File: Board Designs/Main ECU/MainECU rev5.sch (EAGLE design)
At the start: 164 parts, among them Q10 MMBT3904LT3G, Q11 MMBT3904LT3G, Q9 MMBT3904LT3G, X1 CONNECTOR-37, X2 CONNECTOR-4AUTOSPORT, X3 CONNECTOR-4NANO-FIT-VERTICAL-4, X4 CONNECTOR-4NANO-FIT-VERTICAL-4

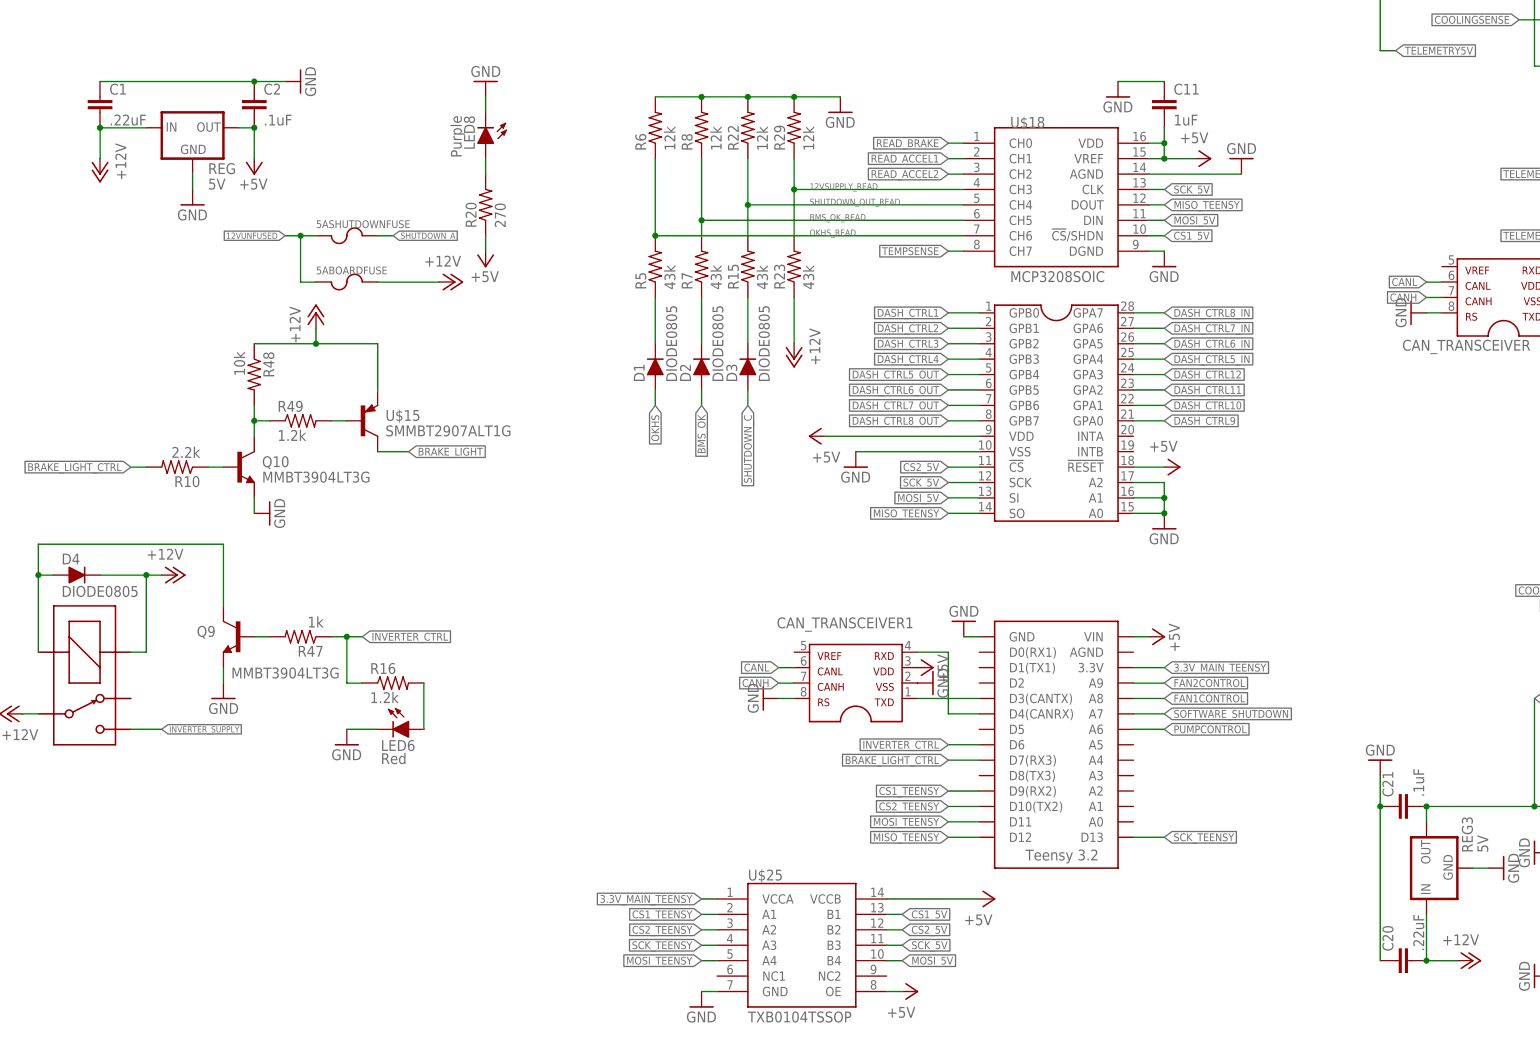
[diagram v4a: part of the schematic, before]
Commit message: Main ECU rev{1-5}: Update values of OKI-78SR capacitors to 10uF
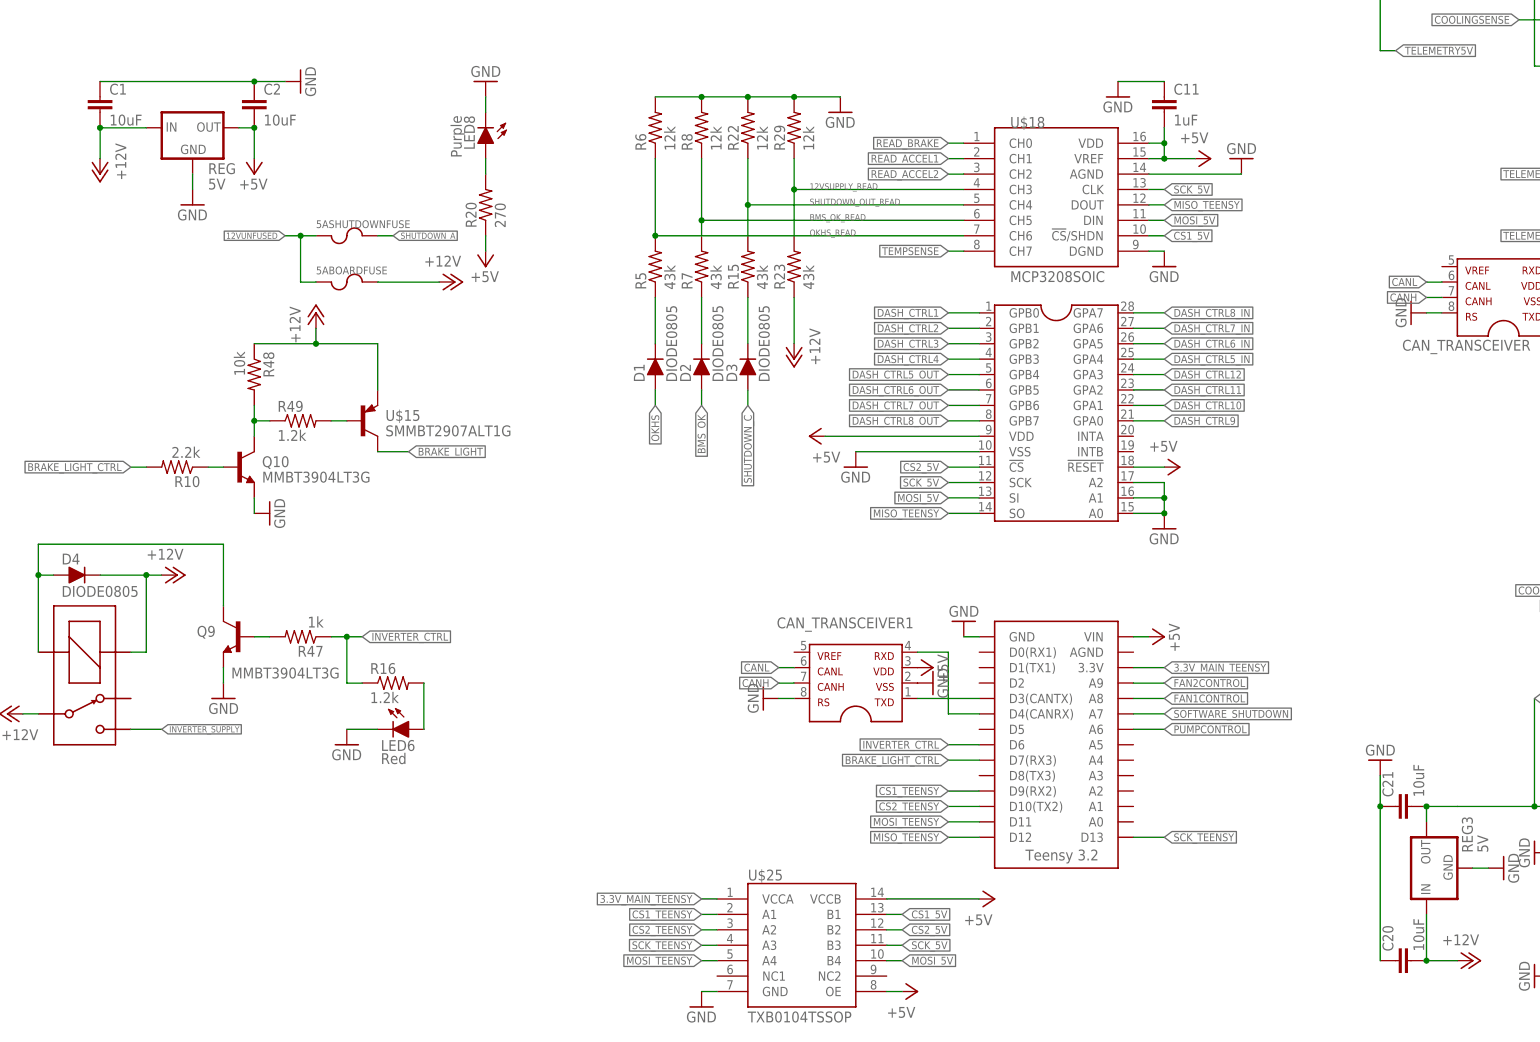
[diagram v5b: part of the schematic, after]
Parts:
- C1, C20: value .22uF -> 10uF
- C2, C21: value .1uF -> 10uF
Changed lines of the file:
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@@
 <part name="REG" library="HyTechDevices" deviceset="OKI-78SR" device="" value="5V"/>
 <part name="GND9" library="HyTechSymbols" deviceset="GND" device=""/>
-<part name="C1" library="HyTechDevices" deviceset="CAP" device="0805" value=".22uF"/>
-<part name="C2" library="HyTechDevices" deviceset="CAP" device="0805" value=".1uF"/>
+<part name="C1" library="HyTechDevices" deviceset="CAP" device="0805" value="10uF"/>
+<part name="C2" library="HyTechDevices" deviceset="CAP" device="0805" value="10uF"/>
 <part name="GND10" library="HyTechSymbols" deviceset="GND" device=""/>
 <part name="P+3" library="supply1" deviceset="+5V" device=""/>
@@
 <part name="REG3" library="HyTechDevices" deviceset="OKI-78SR" device="" value="5V"/>
 <part name="GND39" library="HyTechSymbols" deviceset="GND" device=""/>
-<part name="C20" library="HyTechDevices" deviceset="CAP" device="0805" value=".22uF"/>
-<part name="C21" library="HyTechDevices" deviceset="CAP" device="0805" value=".1uF"/>
+<part name="C20" library="HyTechDevices" deviceset="CAP" device="0805" value="10uF"/>
+<part name="C21" library="HyTechDevices" deviceset="CAP" device="0805" value="10uF"/>
 <part name="GND40" library="HyTechSymbols" deviceset="GND" device=""/>
 <part name="P+32" library="supply1" deviceset="+12V" device=""/>

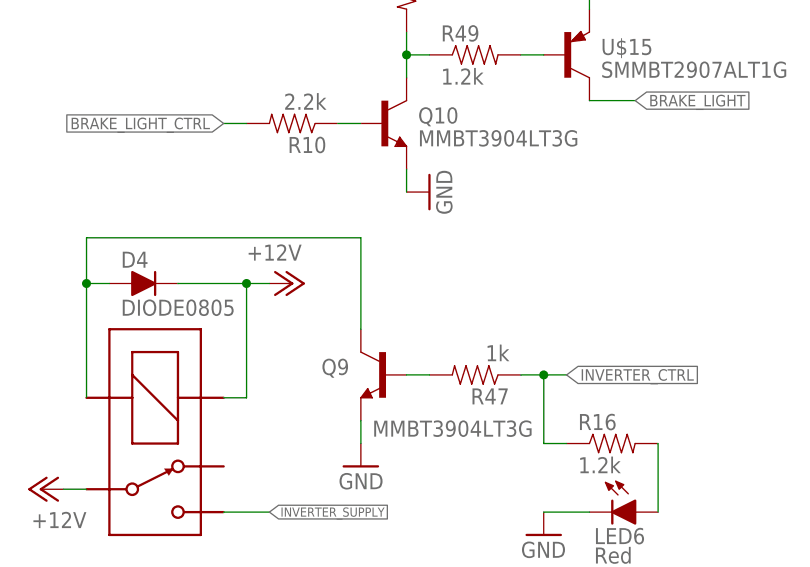
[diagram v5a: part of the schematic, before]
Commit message: Began replacing BJT with mosfets
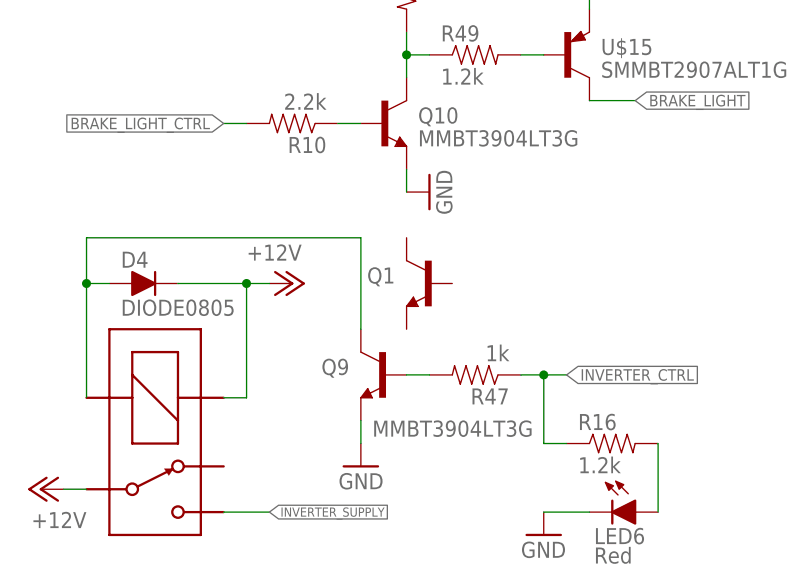
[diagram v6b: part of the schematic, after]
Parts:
- added Q1: (no value), HyTechDevices:DMG3406LSOT
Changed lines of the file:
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@@
 <?xml version="1.0" encoding="utf-8"?>
 <!DOCTYPE eagle SYSTEM "eagle.dtd">
-<eagle version="9.2.2">
+<eagle version="9.3.0">
 <drawing>
 <settings>
-<setting alwaysvectorfont="no"/>
+<setting alwaysvectorfont="yes"/>
 <setting verticaltext="up"/>
 </settings>
-<grid distance="0.1" unitdist="inch" unit="inch" style="lines" multiple="1" display="no" altdistance="0.01" altunitdist="inch" altunit="inch"/>
+<grid distance="0.1" unitdist="inch" unit="inch" style="lines" multiple="1" display="yes" altdistance="0.01" altunitdist="inch" altunit="inch"/>
 <layers>
 <layer number="1" name="Top" color="4" fill="1" visible="no" active="no"/>
@@
 <part name="GND79" library="HyTechSymbols" deviceset="GND" device=""/>
 <part name="FLIP1" library="supply1" library_urn="urn:adsk.eagle:library:371" deviceset="+5V" device=""/>
+<part name="Q1" library="HyTechDevices" deviceset="DMG3406L" device="SOT"/>
 </parts>
 <sheets>
@@
 <attribute name="VALUE" x="312.42" y="5.08" size="1.778" layer="96" rot="MR180"/>
 </instance>
+<instance part="Q1" gate="G$1" x="210.82" y="76.2" smashed="yes" rot="MR0">
+<attribute name="NAME" x="207.01" y="76.2" size="1.778" layer="95" rot="MR0"/>
+<attribute name="VALUE" x="207.01" y="73.66" size="1.778" layer="96" rot="MR0"/>
+</instance>
 </instances>

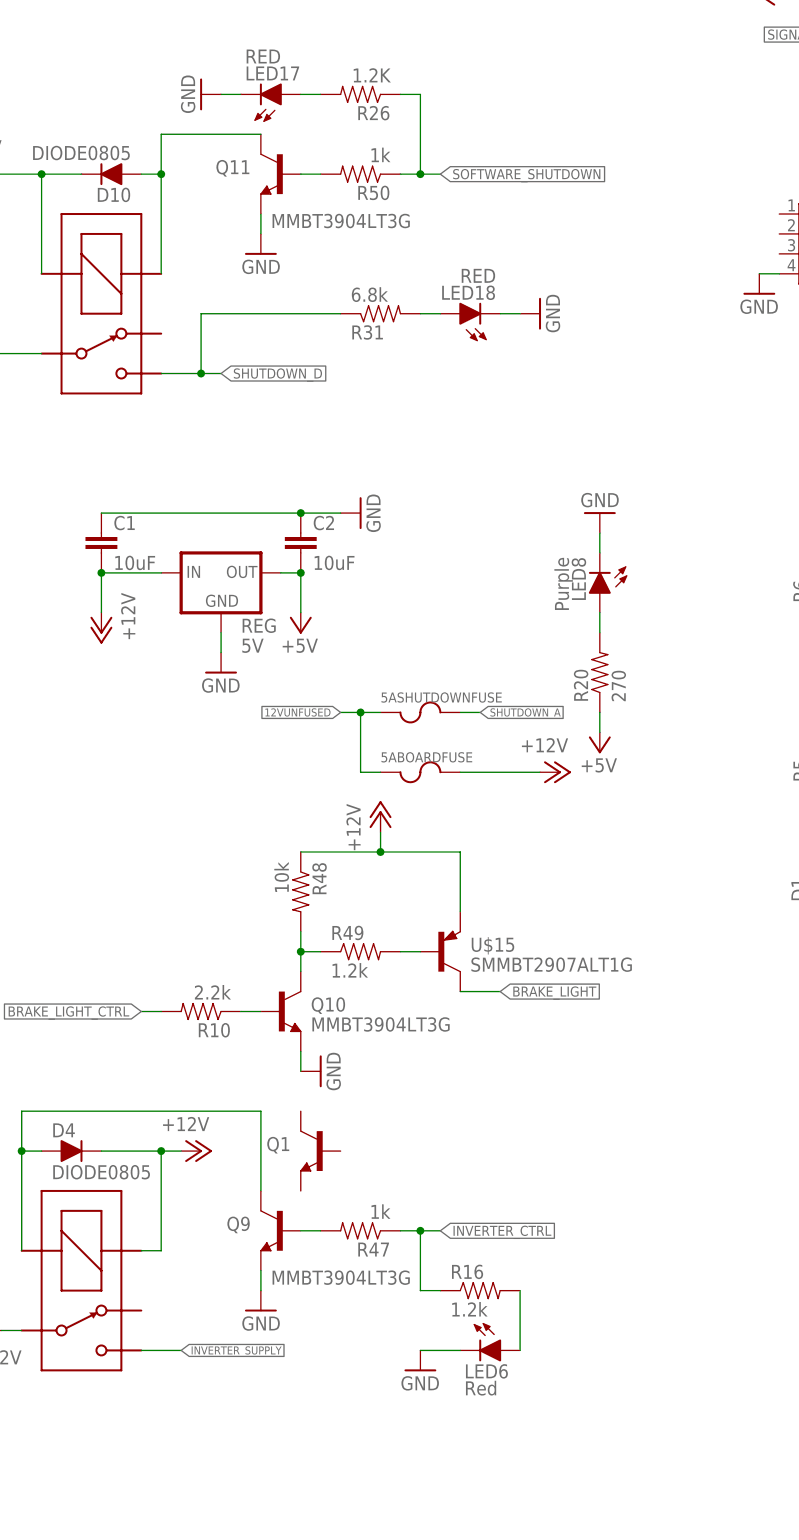
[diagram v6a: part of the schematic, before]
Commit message: Replaced BJTs with MOSFETs, but need to do layout
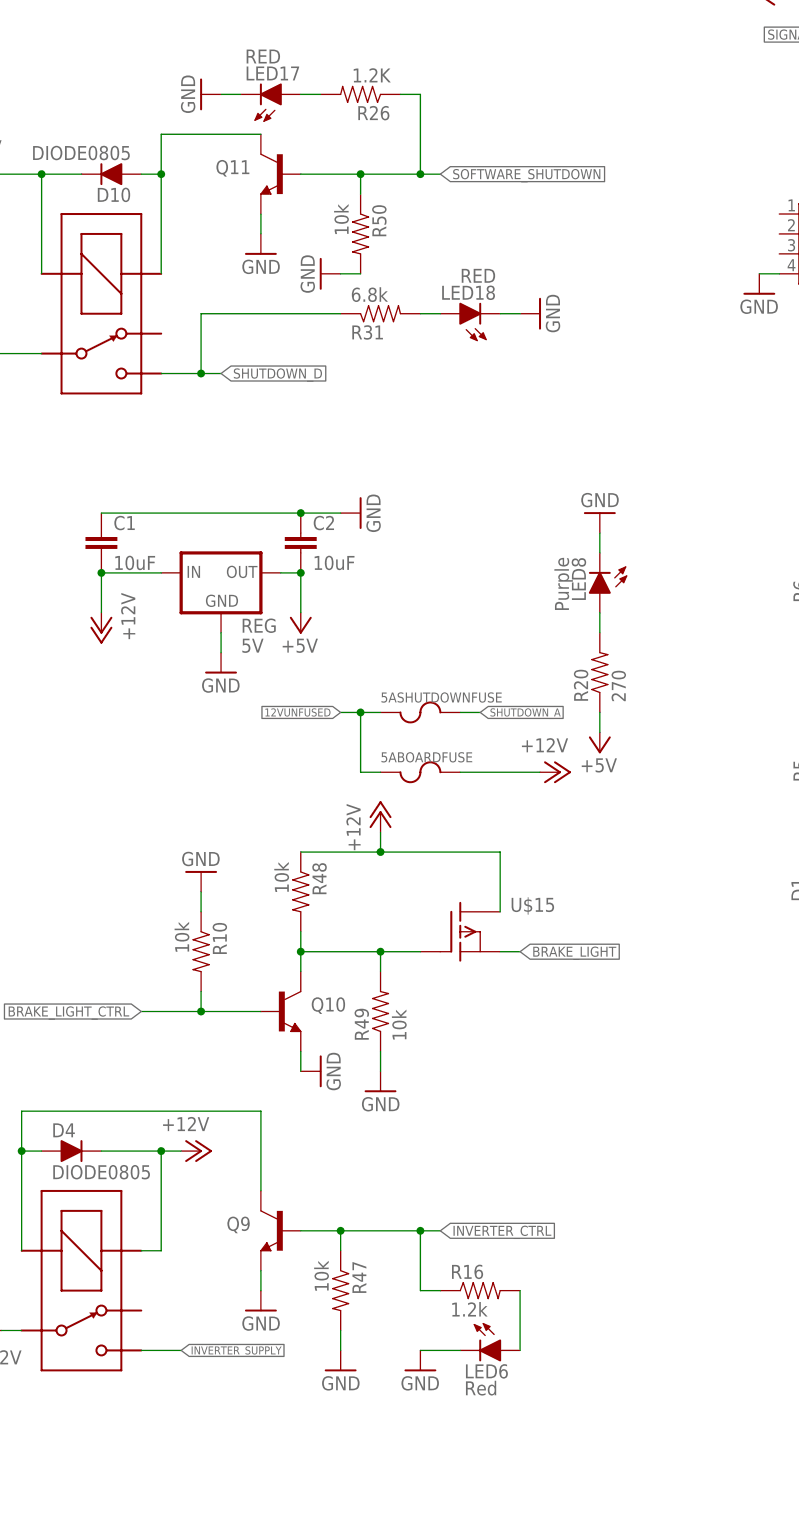
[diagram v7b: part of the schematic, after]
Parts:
- removed Q1: (no value), HyTechDevices:DMG3406LSOT
- Q10, Q11, Q9: value MMBT3904LT3G -> (none); device HyTechDevices:BJT_NPNSOT -> HyTechDevices:DMG3406LSOT
- R10: value 2.2k -> 10k
- R47, R50: value 1k -> 10k
- R49: value 1.2k -> 10k
- U$15: value SMMBT2907ALT1G -> P-CHANNEL_MOSFET_DMP3099L-7; device HyTechDevices:BJT_PNPSOT -> HyTechDevices:P-CHANNEL_MOSFET_DMP3099L-7
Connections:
- removed net N$17: Q10.COLLECTOR, R48.2, R49.1
- removed net N$26: Q11.BASE, R50.2
- removed net N$65: Q9.BASE, R47.2
- removed net N$7: Q10.BASE, R10.1
- net +12V: now also U$15.D; no longer U$15.E
- net BRAKE_LIGHT: now also U$15.S; no longer U$15.C
- net BRAKE_LIGHT_CTRL: now also Q10.BASE
- net GND: now also R10.1, R47.2, R49.1, R50.2
- net INVERTER_CTRL: now also Q9.BASE
- net N$58: now also Q10.COLLECTOR, R48.2, U$15.G; no longer U$15.B
- net SOFTWARE_SHUTDOWN: now also Q11.BASE
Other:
- moved on the sheet: R10, R47, R49, R50
